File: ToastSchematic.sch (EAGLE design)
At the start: 83 parts, among them Q1 DMN63D8LDW, Q2 DMN63D8LDW, Q3 DMN63D8LDW, Q4 DMN63D8LDW, T1 BPX81, T2 BPX81, T3 BPX81, T4 BPX81, T5 BPX81, T6 BPX81, U3 DRV8839_DSS_12, U4 DRV8839_DSS_12

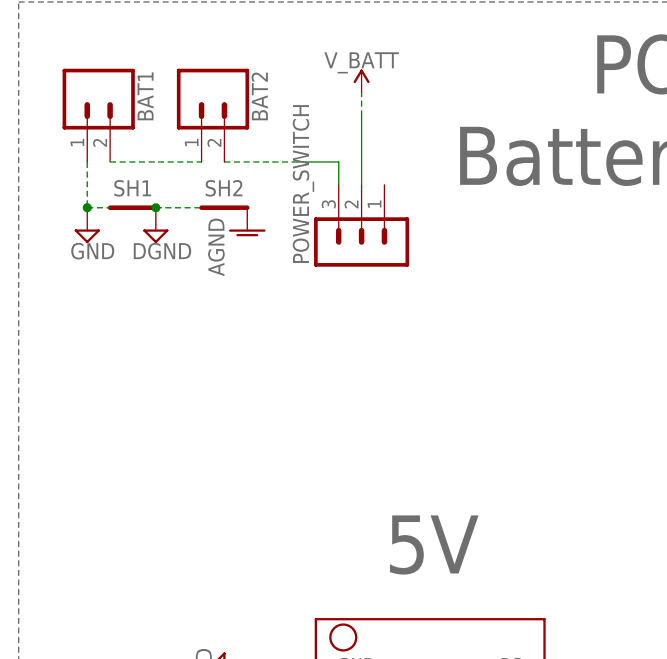
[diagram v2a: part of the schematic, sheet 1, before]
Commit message: Added Ground Splitter
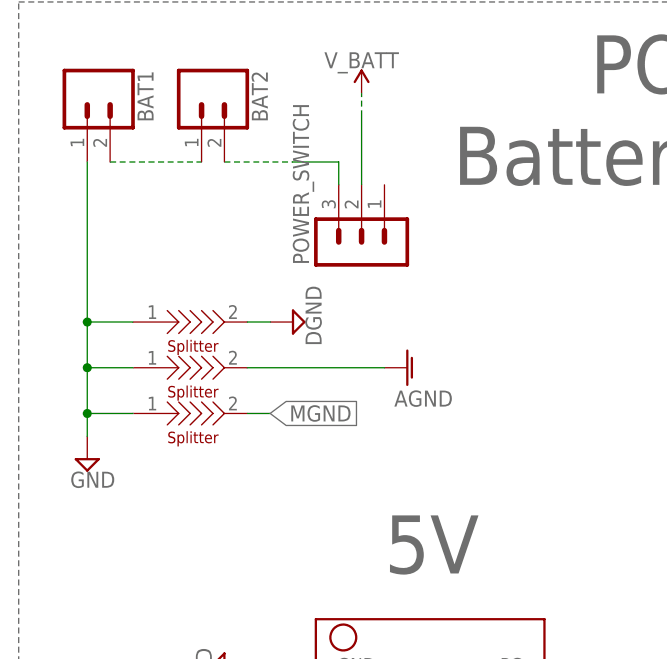
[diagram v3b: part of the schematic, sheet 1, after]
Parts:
- removed SH1, SH2: SHORT-HT5, shorts-old:SHORT-HT5
- added U$5, U$8, U$9: SPLITTER, splitter:SPLITTER
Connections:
- new net MGND: C_M.2, C_M2.2, U$9.2
- net AGND: now also U$8.2; no longer SH2.P$2
- net DGND: now also U$5.2; no longer SH1.P$2, SH2.P$1
- net GND: now also U$5.1, U$8.1, U$9.1; no longer C_M.2, C_M2.2, SH1.P$1
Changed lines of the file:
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@@
 <part name="SUPPLY6" library="supply2" library_urn="urn:adsk.eagle:library:372" deviceset="DGND" device=""/>
 <part name="SUPPLY7" library="supply2" library_urn="urn:adsk.eagle:library:372" deviceset="GND" device=""/>
-<part name="AGND2" library="supply1" library_urn="urn:adsk.eagle:library:371" deviceset="AGND" device=""/>
-<part name="SH1" library="shorts-old" deviceset="SHORT-H" device="T5"/>
-<part name="SH2" library="shorts-old" deviceset="SHORT-H" device="T5"/>
 <part name="SUPPLY8" library="SparkFun-PowerSymbols" deviceset="V_BATT" device=""/>
 <part name="SUPPLY15" library="SparkFun-PowerSymbols" deviceset="V_BATT" device=""/>
@@
 <part name="C_M2" library="rcl" library_urn="urn:adsk.eagle:library:334" deviceset="C-US" device="C0603K" package3d_urn="urn:adsk.eagle:package:23680/2" value="100nF"/>
 <part name="C_M3" library="rcl" library_urn="urn:adsk.eagle:library:334" deviceset="C-US" device="C0603K" package3d_urn="urn:adsk.eagle:package:23680/2" value="100nF"/>
-<part name="SUPPLY36" library="supply2" library_urn="urn:adsk.eagle:library:372" deviceset="GND" device=""/>
 <part name="SUPPLY37" library="supply2" library_urn="urn:adsk.eagle:library:372" deviceset="GND" device=""/>
 <part name="SUPPLY38" library="supply2" library_urn="urn:adsk.eagle:library:372" deviceset="GND" device=""/>
-<part name="SUPPLY39" library="supply2" library_urn="urn:adsk.eagle:library:372" deviceset="GND" device=""/>
 <part name="U$2" library="TPS73633-and-More" deviceset="TPS73633" device=""/>
 <part name="U$3" library="TPS76850SOIC-8" deviceset="TPS76850(SOIC-8)" device=""/>
@@
 <part name="SUPPLY14" library="supply2" library_urn="urn:adsk.eagle:library:372" deviceset="DGND" device=""/>
 <part name="SUPPLY18" library="supply2" library_urn="urn:adsk.eagle:library:372" deviceset="DGND" device=""/>
+<part name="U$5" library="splitter" deviceset="SPLITTER" device=""/>
+<part name="U$8" library="splitter" deviceset="SPLITTER" device=""/>
+<part name="U$9" library="splitter" deviceset="SPLITTER" device=""/>
+<part name="AGND" library="supply1" library_urn="urn:adsk.eagle:library:371" deviceset="AGND" device=""/>
 </parts>
 <sheets>
@@
 <instance part="BAT1" gate="G$1" x="15.24" y="162.56" rot="R270"/>
 <instance part="BAT2" gate="G$1" x="27.94" y="162.56" rot="R270"/>
-<instance part="SUPPLY6" gate="G$1" x="22.86" y="147.32"/>
-<instance part="SUPPLY7" gate="GND" x="15.24" y="147.32"/>
-<instance part="AGND2" gate="VR1" x="33.02" y="147.32"/>
-<instance part="SH1" gate="G$1" x="20.32" y="149.86"/>
-<instance part="SH2" gate="G$1" x="30.48" y="149.86"/>
+<instance part="SUPPLY6" gate="G$1" x="38.1" y="137.16" rot="R90"/>
+<instance part="SUPPLY7" gate="GND" x="15.24" y="121.92"/>
 <instance part="SUPPLY8" gate="G$1" x="45.72" y="162.56"/>
 <instance part="SUPPLY15" gate="G$1" x="17.78" y="83.82" rot="R90"/>
@@
 <instance part="POWER_SWITCH" gate="G$1" x="45.72" y="144.78" rot="R90"/>
 <instance part="SUPPLY16" gate="G$1" x="119.38" y="96.52" rot="R270"/>
+<instance part="U$5" gate="G$1" x="27.94" y="137.16"/>
+<instance part="U$8" gate="G$1" x="27.94" y="132.08"/>
+<instance part="U$9" gate="G$1" x="27.94" y="127"/>
+<instance part="AGND" gate="VR1" x="50.8" y="132.08" rot="R90"/>
 </instances>
 <busses>
@@
 </segment>
 <segment>
-<pinref part="SUPPLY6" gate="G$1" pin="DGND"/>
-<pinref part="SH1" gate="G$1" pin="P$2"/>
-<pinref part="SH2" gate="G$1" pin="P$1"/>
-<wire x1="22.86" y1="149.86" x2="27.94" y2="149.86" width="0.1524" layer="91" style="longdash"/>
-<junction x="22.86" y="149.86"/>
-</segment>
-<segment>
 <pinref part="U$1" gate="G$1" pin="BOOT0"/>
 <pinref part="SUPPLY16" gate="G$1" pin="DGND"/>
 <wire x1="127" y1="96.52" x2="121.92" y2="96.52" width="0.1524" layer="91"/>
+</segment>
+<segment>
+<pinref part="U$5" gate="G$1" pin="2"/>
+<pinref part="SUPPLY6" gate="G$1" pin="DGND"/>
+<wire x1="33.02" y1="137.16" x2="35.56" y2="137.16" width="0.1524" layer="91"/>
 </segment>
 </net>
@@
 </segment>
 <segment>
-<pinref part="AGND2" gate="VR1" pin="AGND"/>
-<pinref part="SH2" gate="G$1" pin="P$2"/>
+<pinref part="U$8" gate="G$1" pin="2"/>
+<wire x1="33.02" y1="132.08" x2="48.26" y2="132.08" width="0.1524" layer="91"/>
+<pinref part="AGND" gate="VR1" pin="AGND"/>
 </segment>
 </net>
@@
 <net name="GND" class="0">
 <segment>
+<pinref part="SUPPLY7" gate="GND" pin="GND"/>
 <pinref part="BAT1" gate="G$1" pin="1"/>
-<pinref part="SUPPLY7" gate="GND" pin="GND"/>
-<wire x1="15.24" y1="154.94" x2="15.24" y2="149.86" width="0.1524" layer="91" style="longdash"/>
-<pinref part="SH1" gate="G$1" pin="P$1"/>
-<wire x1="15.24" y1="149.86" x2="17.78" y2="149.86" width="0.1524" layer="91" style="longdash"/>
-<junction x="15.24" y="149.86"/>
+<wire x1="15.24" y1="154.94" x2="15.24" y2="137.16" width="0.1524" layer="91"/>
+<pinref part="U$9" gate="G$1" pin="1"/>
+<wire x1="15.24" y1="137.16" x2="15.24" y2="132.08" width="0.1524" layer="91"/>
+<wire x1="15.24" y1="132.08" x2="15.24" y2="127" width="0.1524" layer="91"/>
+<wire x1="15.24" y1="127" x2="15.24" y2="124.46" width="0.1524" layer="91"/>
+<wire x1="20.32" y1="127" x2="15.24" y2="127" width="0.1524" layer="91"/>
+<junction x="15.24" y="127"/>
+<pinref part="U$8" gate="G$1" pin="1"/>
+<wire x1="15.24" y1="132.08" x2="20.32" y2="132.08" width="0.1524" layer="91"/>
+<junction x="15.24" y="132.08"/>
+<pinref part="U$5" gate="G$1" pin="1"/>
+<wire x1="20.32" y1="137.16" x2="15.24" y2="137.16" width="0.1524" layer="91"/>
+<junction x="15.24" y="137.16"/>
 </segment>
 <segment>
@@
 <pinref part="U$2" gate="G$1" pin="NR/FB"/>
 <wire x1="68.58" y1="33.02" x2="68.58" y2="35.56" width="0.1524" layer="91"/>
+</segment>
+</net>
+<net name="MGND" class="0">
+<segment>
+<pinref part="U$9" gate="G$1" pin="2"/>
+<wire x1="33.02" y1="127" x2="35.56" y2="127" width="0.1524" layer="91"/>
+<label x="35.56" y="127" size="1.778" layer="95" xref="yes"/>
 </segment>
 </net>
@@
 <instance part="C_M2" gate="G$1" x="27.94" y="119.38" rot="R90"/>
 <instance part="C_M3" gate="G$1" x="17.78" y="152.4" rot="R180"/>
-<instance part="SUPPLY36" gate="GND" x="38.1" y="76.2" rot="R90"/>
 <instance part="SUPPLY37" gate="GND" x="20.32" y="114.3" rot="R180"/>
 <instance part="SUPPLY38" gate="GND" x="22.86" y="157.48" rot="R90"/>
-<instance part="SUPPLY39" gate="GND" x="38.1" y="119.38" rot="R90"/>
 <instance part="S1" gate="G$1" x="73.66" y="27.94"/>
 <instance part="S2" gate="G$1" x="86.36" y="27.94"/>
@@
 </segment>
 <segment>
-<pinref part="C_M" gate="G$1" pin="2"/>
-<pinref part="SUPPLY36" gate="GND" pin="GND"/>
-<wire x1="33.02" y1="76.2" x2="35.56" y2="76.2" width="0.1524" layer="91"/>
-</segment>
-<segment>
 <pinref part="C_M1" gate="G$1" pin="2"/>
 <pinref part="SUPPLY37" gate="GND" pin="GND"/>
@@
 <pinref part="SUPPLY38" gate="GND" pin="GND"/>
 <wire x1="17.78" y1="157.48" x2="20.32" y2="157.48" width="0.1524" layer="91"/>
-</segment>
-<segment>
-<pinref part="C_M2" gate="G$1" pin="2"/>
-<pinref part="SUPPLY39" gate="GND" pin="GND"/>
-<wire x1="33.02" y1="119.38" x2="35.56" y2="119.38" width="0.1524" layer="91"/>
 </segment>
 </net>
@@
 </segment>
 </net>
+<net name="MGND" class="0">
+<segment>
+<pinref part="C_M2" gate="G$1" pin="2"/>
+<wire x1="33.02" y1="119.38" x2="35.56" y2="119.38" width="0.1524" layer="91"/>
+<label x="35.56" y="119.38" size="1.778" layer="95" xref="yes"/>
+</segment>
+<segment>
+<pinref part="C_M" gate="G$1" pin="2"/>
+<wire x1="33.02" y1="76.2" x2="35.56" y2="76.2" width="0.1524" layer="91"/>
+<label x="35.56" y="76.2" size="1.778" layer="95" xref="yes"/>
+</segment>
+</net>

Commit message: Did more routing
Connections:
- net DGND: now also U$8.1
- net GND: no longer C_M1.2, C_M3.2, U$8.1, U3.EPAD, U3.GND, U3.GND_2, U4.EPAD, U4.GND, U4.GND_2
- net MGND: now also C_M1.2, C_M3.2, U3.EPAD, U3.GND, U3.GND_2, U4.EPAD, U4.GND, U4.GND_2
- net MOTOR_LEFT_1: now also U$4.L_MOTOR_B; no longer U$4.L_MOTOR_A
- net MOTOR_LEFT_2: now also U$4.L_MOTOR_A; no longer U$4.L_MOTOR_B
- net MOTOR_RIGHT_1: now also U$4.R_MOTOR_B; no longer U$4.R_MOTOR_A
- net MOTOR_RIGHT_2: now also U$4.R_MOTOR_A; no longer U$4.R_MOTOR_B
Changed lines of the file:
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@@
 <?xml version="1.0" encoding="utf-8"?>
 <!DOCTYPE eagle SYSTEM "eagle.dtd">
-<eagle version="8.4.1">
+<eagle version="8.3.1">
 <drawing>
 <settings>
@@
 <part name="U4" library="DRV8839" deviceset="DRV8839_DSS_12" device=""/>
 <part name="SUPPLY17" library="SparkFun-PowerSymbols" deviceset="V_BATT" device=""/>
-<part name="SUPPLY19" library="supply2" library_urn="urn:adsk.eagle:library:372" deviceset="GND" device=""/>
-<part name="SUPPLY20" library="supply2" library_urn="urn:adsk.eagle:library:372" deviceset="GND" device=""/>
 <part name="+3V9" library="supply1" library_urn="urn:adsk.eagle:library:371" deviceset="+3V3" device=""/>
 <part name="+3V10" library="supply1" library_urn="urn:adsk.eagle:library:371" deviceset="+3V3" device=""/>
@@
 <part name="C_M2" library="rcl" library_urn="urn:adsk.eagle:library:334" deviceset="C-US" device="C0603K" package3d_urn="urn:adsk.eagle:package:23680/2" value="100nF"/>
 <part name="C_M3" library="rcl" library_urn="urn:adsk.eagle:library:334" deviceset="C-US" device="C0603K" package3d_urn="urn:adsk.eagle:package:23680/2" value="100nF"/>
-<part name="SUPPLY37" library="supply2" library_urn="urn:adsk.eagle:library:372" deviceset="GND" device=""/>
-<part name="SUPPLY38" library="supply2" library_urn="urn:adsk.eagle:library:372" deviceset="GND" device=""/>
 <part name="U$2" library="TPS73633-and-More" deviceset="TPS73633" device=""/>
 <part name="U$3" library="TPS76850SOIC-8" deviceset="TPS76850(SOIC-8)" device=""/>
@@
 <pinref part="SUPPLY6" gate="G$1" pin="DGND"/>
 <wire x1="33.02" y1="137.16" x2="35.56" y2="137.16" width="0.1524" layer="91"/>
+<wire x1="33.02" y1="137.16" x2="33.02" y2="134.62" width="0.1524" layer="91"/>
+<junction x="33.02" y="137.16"/>
+<pinref part="U$8" gate="G$1" pin="1"/>
+<wire x1="33.02" y1="134.62" x2="20.32" y2="134.62" width="0.1524" layer="91"/>
+<wire x1="20.32" y1="134.62" x2="20.32" y2="132.08" width="0.1524" layer="91"/>
 </segment>
 </net>
@@
 <wire x1="15.24" y1="154.94" x2="15.24" y2="137.16" width="0.1524" layer="91"/>
 <pinref part="U$9" gate="G$1" pin="1"/>
-<wire x1="15.24" y1="137.16" x2="15.24" y2="132.08" width="0.1524" layer="91"/>
-<wire x1="15.24" y1="132.08" x2="15.24" y2="127" width="0.1524" layer="91"/>
+<wire x1="15.24" y1="137.16" x2="15.24" y2="127" width="0.1524" layer="91"/>
 <wire x1="15.24" y1="127" x2="15.24" y2="124.46" width="0.1524" layer="91"/>
 <wire x1="20.32" y1="127" x2="15.24" y2="127" width="0.1524" layer="91"/>
 <junction x="15.24" y="127"/>
-<pinref part="U$8" gate="G$1" pin="1"/>
-<wire x1="15.24" y1="132.08" x2="20.32" y2="132.08" width="0.1524" layer="91"/>
-<junction x="15.24" y="132.08"/>
 <pinref part="U$5" gate="G$1" pin="1"/>
 <wire x1="20.32" y1="137.16" x2="15.24" y2="137.16" width="0.1524" layer="91"/>
@@
 <instance part="U4" gate="A" x="25.4" y="101.6"/>
 <instance part="SUPPLY17" gate="G$1" x="25.4" y="149.86"/>
-<instance part="SUPPLY19" gate="GND" x="91.44" y="154.94" rot="R180"/>
-<instance part="SUPPLY20" gate="GND" x="91.44" y="109.22" rot="R180"/>
 <instance part="+3V9" gate="G$1" x="20.32" y="129.54" rot="R90"/>
 <instance part="+3V10" gate="G$1" x="20.32" y="83.82" rot="R90"/>
@@
 <instance part="C_M2" gate="G$1" x="27.94" y="119.38" rot="R90"/>
 <instance part="C_M3" gate="G$1" x="17.78" y="152.4" rot="R180"/>
-<instance part="SUPPLY37" gate="GND" x="20.32" y="114.3" rot="R180"/>
-<instance part="SUPPLY38" gate="GND" x="22.86" y="157.48" rot="R90"/>
 <instance part="S1" gate="G$1" x="73.66" y="27.94"/>
 <instance part="S2" gate="G$1" x="86.36" y="27.94"/>
@@
 </segment>
 </net>
-<net name="GND" class="0">
-<segment>
-<pinref part="U4" gate="A" pin="GND_2"/>
-<pinref part="U4" gate="A" pin="GND"/>
-<wire x1="91.44" y1="99.06" x2="91.44" y2="101.6" width="0.1524" layer="91"/>
-<pinref part="U4" gate="A" pin="EPAD"/>
-<wire x1="91.44" y1="104.14" x2="91.44" y2="101.6" width="0.1524" layer="91"/>
-<junction x="91.44" y="101.6"/>
-<pinref part="SUPPLY20" gate="GND" pin="GND"/>
-<wire x1="91.44" y1="106.68" x2="91.44" y2="104.14" width="0.1524" layer="91"/>
-<junction x="91.44" y="104.14"/>
-</segment>
-<segment>
-<pinref part="SUPPLY19" gate="GND" pin="GND"/>
-<pinref part="U3" gate="A" pin="EPAD"/>
-<wire x1="91.44" y1="152.4" x2="91.44" y2="149.86" width="0.1524" layer="91"/>
-<pinref part="U3" gate="A" pin="GND"/>
-<wire x1="91.44" y1="149.86" x2="91.44" y2="147.32" width="0.1524" layer="91"/>
-<junction x="91.44" y="149.86"/>
-<pinref part="U3" gate="A" pin="GND_2"/>
-<wire x1="91.44" y1="147.32" x2="91.44" y2="144.78" width="0.1524" layer="91"/>
-<junction x="91.44" y="147.32"/>
-</segment>
-<segment>
-<pinref part="C_M1" gate="G$1" pin="2"/>
-<pinref part="SUPPLY37" gate="GND" pin="GND"/>
-<wire x1="20.32" y1="109.22" x2="20.32" y2="111.76" width="0.1524" layer="91"/>
-</segment>
-<segment>
-<pinref part="C_M3" gate="G$1" pin="2"/>
-<pinref part="SUPPLY38" gate="GND" pin="GND"/>
-<wire x1="17.78" y1="157.48" x2="20.32" y2="157.48" width="0.1524" layer="91"/>
-</segment>
-</net>
 <net name="M_R_F" class="0">
 <segment>
@@
 </segment>
 <segment>
-<pinref part="U$4" gate="G$1" pin="R_MOTOR_A"/>
-<wire x1="149.86" y1="195.58" x2="149.86" y2="185.42" width="0.1524" layer="91"/>
-<label x="149.86" y="185.42" size="1.778" layer="95" xref="yes"/>
+<label x="157.48" y="190.5" size="1.778" layer="95" xref="yes"/>
+<pinref part="U$4" gate="G$1" pin="R_MOTOR_B"/>
+<wire x1="157.48" y1="195.58" x2="157.48" y2="190.5" width="0.1524" layer="91"/>
 </segment>
 </net>
@@
 </segment>
 <segment>
-<pinref part="U$4" gate="G$1" pin="R_MOTOR_B"/>
-<wire x1="157.48" y1="195.58" x2="157.48" y2="187.96" width="0.1524" layer="91"/>
-<label x="157.48" y="187.96" size="1.778" layer="95" xref="yes"/>
+<label x="149.86" y="185.42" size="1.778" layer="95" xref="yes"/>
+<pinref part="U$4" gate="G$1" pin="R_MOTOR_A"/>
+<wire x1="149.86" y1="195.58" x2="149.86" y2="185.42" width="0.1524" layer="91"/>
 </segment>
 </net>
@@
 </segment>
 <segment>
-<pinref part="U$4" gate="G$1" pin="L_MOTOR_B"/>
-<wire x1="17.78" y1="195.58" x2="17.78" y2="190.5" width="0.1524" layer="91"/>
-<label x="17.78" y="190.5" size="1.778" layer="95" xref="yes"/>
+<wire x1="10.16" y1="195.58" x2="10.16" y2="185.42" width="0.1524" layer="91"/>
+<label x="10.16" y="185.42" size="1.778" layer="95" xref="yes"/>
+<pinref part="U$4" gate="G$1" pin="L_MOTOR_A"/>
 </segment>
 </net>
@@
 </segment>
 <segment>
-<pinref part="U$4" gate="G$1" pin="L_MOTOR_A"/>
-<wire x1="10.16" y1="195.58" x2="10.16" y2="185.42" width="0.1524" layer="91"/>
-<label x="10.16" y="185.42" size="1.778" layer="95" xref="yes"/>
+<label x="17.78" y="190.5" size="1.778" layer="95" xref="yes"/>
+<pinref part="U$4" gate="G$1" pin="L_MOTOR_B"/>
+<wire x1="17.78" y1="195.58" x2="17.78" y2="190.5" width="0.1524" layer="91"/>
 </segment>
 </net>
@@
 <label x="35.56" y="76.2" size="1.778" layer="95" xref="yes"/>
 </segment>
-</net>
+<segment>
+<pinref part="C_M1" gate="G$1" pin="2"/>
+<wire x1="20.32" y1="109.22" x2="20.32" y2="111.76" width="0.1524" layer="91"/>
+<label x="20.32" y="111.76" size="1.778" layer="95" xref="yes"/>
+</segment>
+<segment>
+<pinref part="U4" gate="A" pin="GND_2"/>
+<pinref part="U4" gate="A" pin="GND"/>
+<wire x1="91.44" y1="99.06" x2="91.44" y2="101.6" width="0.1524" layer="91"/>
+<pinref part="U4" gate="A" pin="EPAD"/>
+<wire x1="91.44" y1="104.14" x2="91.44" y2="101.6" width="0.1524" layer="91"/>
+<junction x="91.44" y="101.6"/>
+<wire x1="91.44" y1="106.68" x2="91.44" y2="104.14" width="0.1524" layer="91"/>
+<junction x="91.44" y="104.14"/>
+<label x="91.44" y="106.68" size="1.778" layer="95" rot="R90" xref="yes"/>
+</segment>
+<segment>
+<pinref part="U3" gate="A" pin="EPAD"/>
+<wire x1="91.44" y1="152.4" x2="91.44" y2="149.86" width="0.1524" layer="91"/>
+<pinref part="U3" gate="A" pin="GND"/>
+<wire x1="91.44" y1="149.86" x2="91.44" y2="147.32" width="0.1524" layer="91"/>
+<junction x="91.44" y="149.86"/>
+<pinref part="U3" gate="A" pin="GND_2"/>
+<wire x1="91.44" y1="147.32" x2="91.44" y2="144.78" width="0.1524" layer="91"/>
+<junction x="91.44" y="147.32"/>
+<label x="91.44" y="152.4" size="1.778" layer="95" rot="R90" xref="yes"/>
+</segment>
+<segment>
+<pinref part="C_M3" gate="G$1" pin="2"/>
+<wire x1="17.78" y1="157.48" x2="20.32" y2="157.48" width="0.1524" layer="91"/>
+<label x="20.32" y="157.48" size="1.778" layer="95" xref="yes"/>
+</segment>
+</net>

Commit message: Minor Fixes
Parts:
- removed C_BUZ: 100nF, rcl:C-USC0603K
- added D1: (no value), adafruit:DIODESOD-323F
- added LED7: (no value), led:LED5MM
- added R1: (no value), rcl:R-US_R0603
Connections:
- removed net N$13 (its old number): Q4B.S, SPK1.-
- removed net N$16 (its old number): LED1.C, Q1B.S
- removed net N$22: LED2.C, Q1A.S
- removed net N$24: LED4.C, Q2A.S
- removed net N$25: LED5.C, Q3B.S
- removed net N$26: LED6.C, Q3A.S
- new net DISP_CE: U$6.!CE
- new net N$11: LED2.C, Q1A.D
- new net N$12: LED3.C, Q2B.D
- new net N$15: LED6.C, Q3A.D
- new net N$18: LED4.C, Q2A.D
- new net N$20: LED5.C, Q3B.D
- new net N$21: LED7.A, R1.2
- new net N$9: LED1.C, Q1B.D
- net +3V3: now also D1.C; no longer C_BUZ.1
- net DGND: now also C_M.2, C_M2.2, Q1A.S, Q1B.S, Q2A.S, Q2B.S, Q3A.S, Q3B.S, Q4B.S; no longer C15.2, C_BUZ.2, Q1A.D, Q1B.D, Q2A.D, Q2B.D, Q3A.D, Q3B.D, Q4B.D, R23.2, U$6.!CE, U$8.1
- net GND: now also LED7.C, U$8.1
- net MGND: no longer C_M.2, C_M2.2
- net N$23: now also D1.A, Q4B.D, SPK1.-; no longer LED3.C, Q2B.S
- net V_BATT: now also R1.1
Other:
- moved on the sheet: C13, C14, C16, C17, C18, Q1A, Q1B, Q2A, Q2B, Q3A, Q3B, Q4B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
